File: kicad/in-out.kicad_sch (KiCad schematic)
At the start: 67 parts, among them U3 LM5106MM

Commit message: Most of the main board is done
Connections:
- net C2: no longer names the net of J?.2, R?.1
- net C2: no longer J?.2, R?.1
- removed net C3: J?.2, J?.2, J?.3, J?.3, J?.3, J?.3, TC?.1 (+), TC?.1 (+), TC?.1 (+), TC?.1 (+)
- net VOUT_{SEN} renamed V_{OUT}
- new net: J?.2, J?.3, TC?.1 (+) (x2)
- new net: J?.3, TC?.1 (+) (x2)
- new net: J?.2, R?.1
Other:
- note added: "C1"
- note added: "C1/C2"
- note added: "C2"
- note added: "C3"
- moved on the sheet: R?
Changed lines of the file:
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@@
     (stroke (width 0) (type default))
   )
-  (wire (pts (xy 29.21 35.56) (xy 29.21 33.02))
+  (wire (pts (xy 33.02 35.56) (xy 33.02 31.75))
     (stroke (width 0) (type default))
   )
@@
     (stroke (width 0) (type default))
   )
-  (wire (pts (xy 29.21 22.86) (xy 25.4 22.86))
+  (wire (pts (xy 33.02 21.59) (xy 29.21 21.59))
     (stroke (width 0) (type default))
   )
@@
     (stroke (width 0) (type default))
   )
-  (wire (pts (xy 26.67 67.31) (xy 22.86 67.31))
+  (wire (pts (xy 30.48 66.04) (xy 26.67 66.04))
     (stroke (width 0) (type default))
   )
@@
     (stroke (width 0) (type default))
   )
-  (wire (pts (xy 29.21 25.4) (xy 29.21 22.86))
+  (wire (pts (xy 33.02 24.13) (xy 33.02 21.59))
     (stroke (width 0) (type default))
   )
@@
     (stroke (width 0) (type default))
   )
-  (wire (pts (xy 26.67 80.01) (xy 26.67 77.47))
+  (wire (pts (xy 30.48 80.01) (xy 30.48 76.2))
     (stroke (width 0) (type default))
   )
@@
     (stroke (width 0) (type default))
   )
-  (wire (pts (xy 26.67 69.85) (xy 26.67 67.31))
+  (wire (pts (xy 30.48 68.58) (xy 30.48 66.04))
     (stroke (width 0) (type default))
   )
@@
     (stroke (width 0) (type default))
   )
-  (wire (pts (xy 26.67 80.01) (xy 30.48 80.01))
-    (stroke (width 0) (type default))
-  )
   (wire (pts (xy 229.87 49.53) (xy 233.68 49.53))
     (stroke (width 0) (type default))
@@
     (stroke (width 0) (type default))
   )
-  (wire (pts (xy 29.21 35.56) (xy 33.02 35.56))
-    (stroke (width 0) (type default))
-  )
   (wire (pts (xy 33.02 35.56) (xy 33.02 39.37))
     (stroke (width 0) (type default))
@@
     (stroke (width 0) (type default))
   )
-  (text "C245" (at 57.15 135.89 0)
-    (effects (font (size 1.27 1.27) (thickness 0.254) bold) (justify left bottom))
+  (text "C3" (at 43.18 137.16 0)
+    (effects (font (size 1.27 1.27)) (justify left bottom))
   )
-  (text "C210" (at 96.52 163.83 0)
-    (effects (font (size 1.27 1.27) (thickness 0.254) bold) (justify right bottom))
+  (text "C3" (at 43.18 167.64 0)
+    (effects (font (size 1.27 1.27)) (justify left bottom))
   )
-  (text "C470" (at 57.15 166.37 0)
-    (effects (font (size 1.27 1.27) (thickness 0.254) bold) (justify left bottom))
+  (text "C2" (at 43.18 140.97 0)
+    (effects (font (size 1.27 1.27)) (justify left bottom))
   )
-  (text "C115" (at 96.52 132.08 0)
-    (effects (font (size 1.27 1.27) (thickness 0.254) bold) (justify right bottom))
+  (text "C245" (at 57.15 135.89 0)
+    (effects (font (size 1.27 1.27) (thickness 0.254) bold) (justify left bottom))
   )
-  (label "C2" (at 43.18 171.45 0) (fields_autoplaced)
+  (text "C1/C2" (at 106.68 156.21 0)
     (effects (font (size 1.27 1.27)) (justify left bottom))
   )
-  (label "C3" (at 43.18 137.16 0) (fields_autoplaced)
+  (text "C1" (at 43.18 152.4 0)
     (effects (font (size 1.27 1.27)) (justify left bottom))
   )
-  (label "C3" (at 43.18 167.64 0) (fields_autoplaced)
+  (text "C3" (at 115.57 165.1 0)
     (effects (font (size 1.27 1.27)) (justify left bottom))
   )
-  (label "C1{slash}C2" (at 106.68 187.96 0) (fields_autoplaced)
-    (effects (font (size 1.27 1.27)) (justify left bottom))
+  (text "C210" (at 96.52 163.83 0)
+    (effects (font (size 1.27 1.27) (thickness 0.254) bold) (justify right bottom))
   )
-  (label "C3" (at 115.57 133.35 0) (fields_autoplaced)
-    (effects (font (size 1.27 1.27)) (justify left bottom))
+  (text "C470" (at 57.15 166.37 0)
+    (effects (font (size 1.27 1.27) (thickness 0.254) bold) (justify left bottom))
   )
-  (label "C3" (at 115.57 165.1 0) (fields_autoplaced)
+  (text "C2" (at 43.18 171.45 0)
     (effects (font (size 1.27 1.27)) (justify left bottom))
   )
-  (label "C1" (at 43.18 152.4 0) (fields_autoplaced)
-    (effects (font (size 1.27 1.27)) (justify left bottom))
+  (text "C115" (at 96.52 132.08 0)
+    (effects (font (size 1.27 1.27) (thickness 0.254) bold) (justify right bottom))
   )
-  (label "C1" (at 43.18 182.88 0) (fields_autoplaced)
+  (text "C1/C2" (at 106.68 187.96 0)
     (effects (font (size 1.27 1.27)) (justify left bottom))
   )
-  (label "C1{slash}C2" (at 106.68 156.21 0) (fields_autoplaced)
+  (text "C1" (at 43.18 182.88 0)
     (effects (font (size 1.27 1.27)) (justify left bottom))
   )
-  (label "C2" (at 43.18 140.97 0) (fields_autoplaced)
+  (text "C3" (at 115.57 133.35 0)
     (effects (font (size 1.27 1.27)) (justify left bottom))
   )
@@
     (effects (font (size 1.27 1.27)) (justify left))
   )
-  (hierarchical_label "HNDL_{SEN}" (shape input) (at 25.4 22.86 180) (fields_autoplaced)
+  (hierarchical_label "HNDL_{SEN}" (shape input) (at 29.21 21.59 180) (fields_autoplaced)
     (effects (font (size 1.27 1.27)) (justify right))
   )
@@
     (effects (font (size 1.27 1.27)) (justify left))
   )
-  (hierarchical_label "VOUT_{SEN}" (shape input) (at 41.91 57.15 180) (fields_autoplaced)
+  (hierarchical_label "V_{OUT}" (shape input) (at 41.91 57.15 180) (fields_autoplaced)
     (effects (font (size 1.27 1.27)) (justify right))
   )
@@
     (effects (font (size 1.27 1.27)) (justify left))
   )
-  (hierarchical_label "SLEEP_{SEN}" (shape input) (at 22.86 67.31 180) (fields_autoplaced)
+  (hierarchical_label "SLEEP_{SEN}" (shape input) (at 26.67 66.04 180) (fields_autoplaced)
     (effects (font (size 1.27 1.27)) (justify right))
   )
@@
     )
   )
-  (symbol (lib_id "Device:R") (at 29.21 29.21 0) (unit 1)
+  (symbol (lib_id "Device:R") (at 33.02 27.94 0) (unit 1)
     (in_bom yes) (on_board yes) (dnp no)
-    (property "Reference" "R?" (at 30.48 26.67 0)
+    (property "Reference" "R?" (at 34.29 25.4 0)
       (effects (font (size 1.27 1.27)) (justify left))
     )
-    (property "Value" "220" (at 30.48 31.75 0)
+    (property "Value" "220" (at 34.29 30.48 0)
       (effects (font (size 1.27 1.27)) (justify left))
     )
-    (property "Footprint" "Resistor_SMD:R_0603_1608Metric_Pad0.98x0.95mm_HandSolder" (at 27.432 29.21 90)
+    (property "Footprint" "Resistor_SMD:R_0603_1608Metric_Pad0.98x0.95mm_HandSolder" (at 31.242 27.94 90)
       (effects (font (size 1.27 1.27)) hide)
     )
-    (property "Datasheet" "~" (at 29.21 29.21 0)
+    (property "Datasheet" "~" (at 33.02 27.94 0)
       (effects (font (size 1.27 1.27)) hide)
     )
@@
     )
   )
-  (symbol (lib_id "Device:R") (at 26.67 73.66 0) (unit 1)
+  (symbol (lib_id "Device:R") (at 30.48 72.39 0) (unit 1)
     (in_bom yes) (on_board yes) (dnp no)
-    (property "Reference" "R?" (at 27.94 71.12 0)
+    (property "Reference" "R?" (at 31.75 69.85 0)
       (effects (font (size 1.27 1.27)) (justify left))
     )
-    (property "Value" "220" (at 27.94 76.2 0)
+    (property "Value" "220" (at 31.75 74.93 0)
       (effects (font (size 1.27 1.27)) (justify left))
     )
-    (property "Footprint" "Resistor_SMD:R_0603_1608Metric_Pad0.98x0.95mm_HandSolder" (at 24.892 73.66 90)
+    (property "Footprint" "Resistor_SMD:R_0603_1608Metric_Pad0.98x0.95mm_HandSolder" (at 28.702 72.39 90)
       (effects (font (size 1.27 1.27)) hide)
     )
-    (property "Datasheet" "~" (at 26.67 73.66 0)
+    (property "Datasheet" "~" (at 30.48 72.39 0)
       (effects (font (size 1.27 1.27)) hide)
     )
@@
   )
   (symbol (lib_id "PCM_Diode_Schottky_AKL:B0530WS") (at 63.5 80.01 0) (unit 1)
-    (in_bom yes) (on_board yes) (dnp no) (fields_autoplaced)
+    (in_bom yes) (on_board yes) (dnp no)
     (property "Reference" "D9" (at 63.8175 74.93 0)
       (effects (font (size 1.27 1.27)))

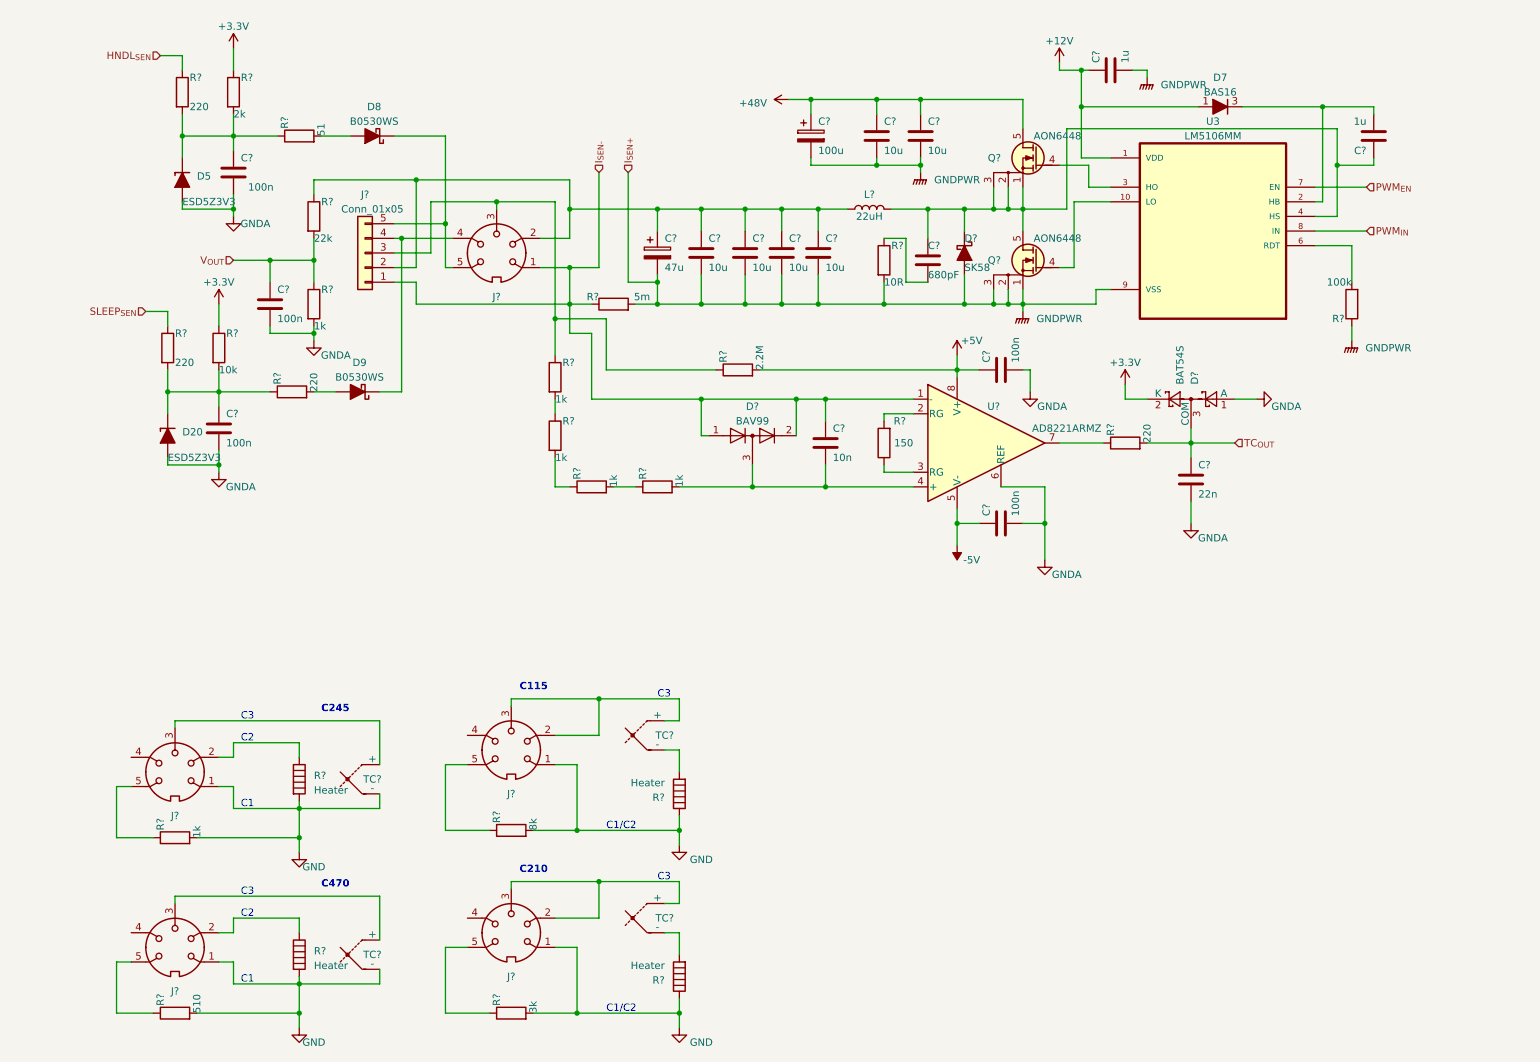
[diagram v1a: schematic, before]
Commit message: Main board: add BT
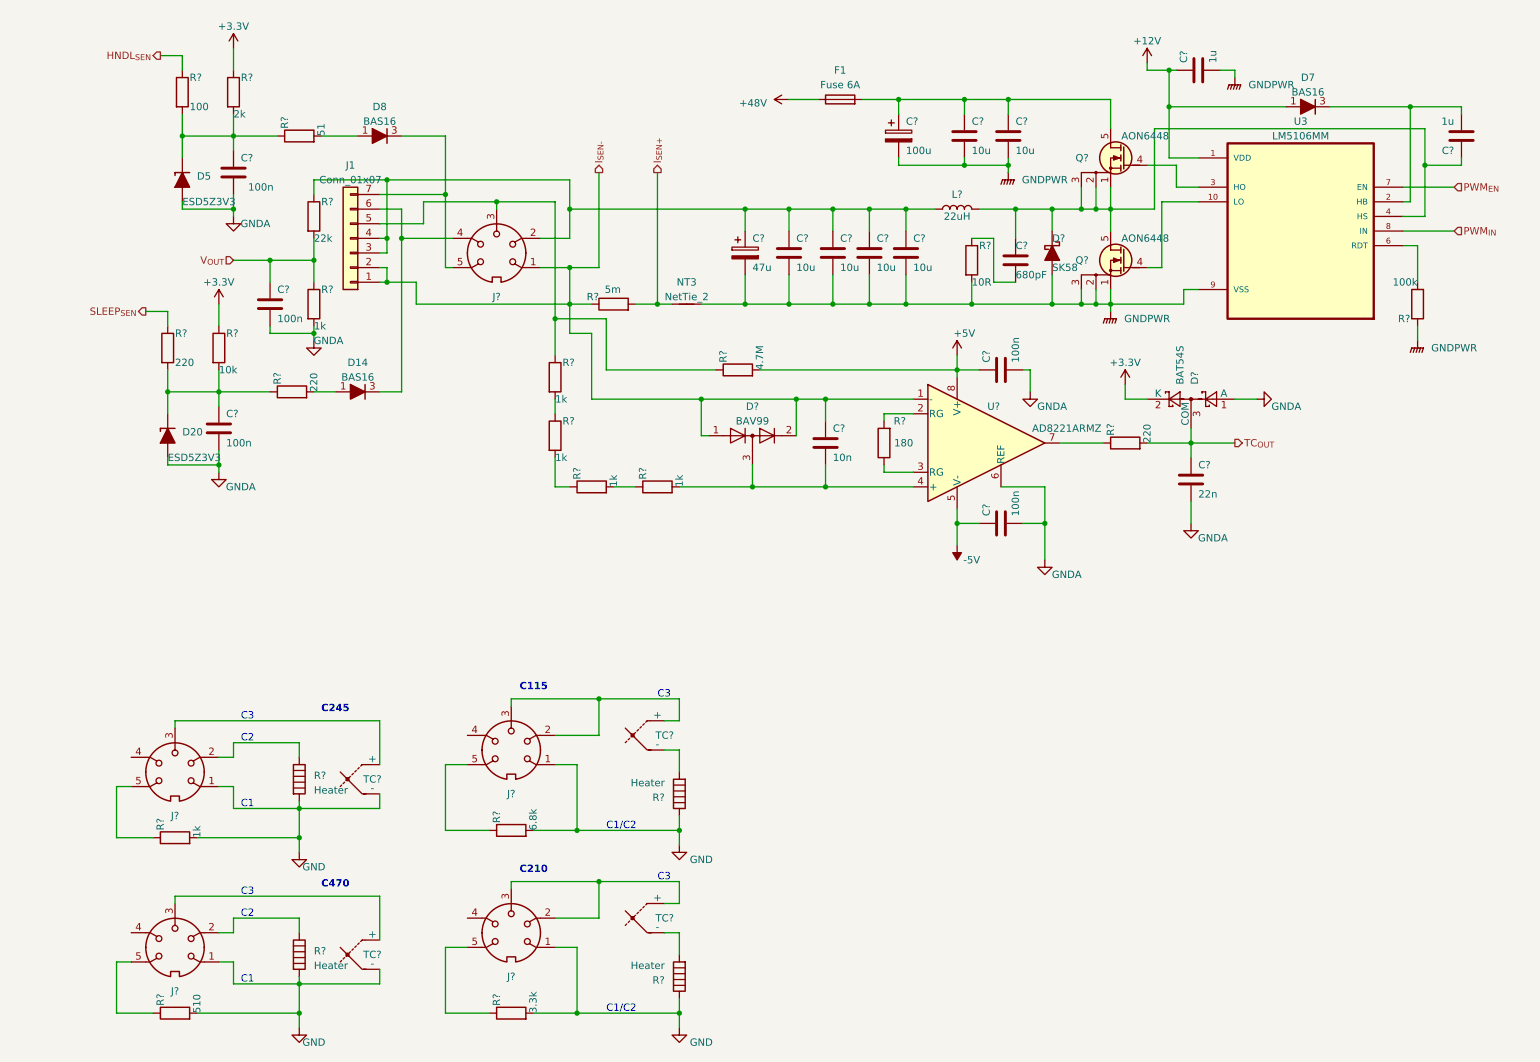
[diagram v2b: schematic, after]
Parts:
- removed D8, D9: B0530WS, PCM_Diode_SMD_AKL:D_SOD-323F, symbol PCM_Diode_Schottky_AKL:B0530WS
- removed J?: Conn_01x05, Connector_JST:JST_EH_B5B-EH-A_1x05_P2.50mm_Vertical, symbol Connector_Generic:Conn_01x05
- added D14, D8: BAS16, Package_TO_SOT_SMD_AKL:SOT-23, symbol Diode_AKL:BAS16
- added F1: Fuse 6A, Fuse:Fuseholder_Littelfuse_Nano2_154x, symbol Device:Fuse
- added J1: Conn_01x07, Connector_JST:JST_EH_B7B-EH-A_1x07_P2.50mm_Vertical, symbol Connector_Generic:Conn_01x07
- added NT3: NetTie_2, NetTie:NetTie-2_SMD_Pad2.0mm, symbol Device:NetTie_2
- C?: footprint Capacitor_SMD:C_0805_2012Metric -> Capacitor_THT:C_Radial_D8.0mm_H11.5mm_P3.50mm
- C? (x5): footprint Capacitor_SMD:C_0805_2012Metric -> Capacitor_SMD:C_0603_1608Metric_Pad1.08x0.95mm_HandSolder
- C?: footprint Inductor_SMD:L_Bourns_SRP1770TA_16.9x16.9mm -> Capacitor_THT:C_Radial_D8.0mm_H11.5mm_P3.50mm
- D20: footprint PCM_Diode_SMD_AKL:D_SOD-523 -> Diode_SMD:D_SOD-523; symbol PCM_Diode_TVS_AKL:ESD5Z3V3 -> Diode_TVS_AKL:ESD5Z3V3
- D5: footprint PCM_Diode_SMD_AKL:D_SOD-523_TVS -> Diode_SMD_AKL:D_SOD-523_TVS; symbol PCM_Diode_TVS_AKL:ESD5Z3V3 -> Diode_TVS_AKL:ESD5Z3V3
- D7: footprint PCM_Package_TO_SOT_SMD_AKL:SOT-23 -> Package_TO_SOT_SMD_AKL:SOT-23; symbol PCM_Diode_AKL:BAS16 -> Diode_AKL:BAS16
- D?: footprint PCM_Diode_SMD_AKL:D_SMB-SMC_Universal -> Diode_SMD_AKL:D_SMB-SMC_Universal; symbol PCM_Diode_Schottky_AKL:SK58 -> Diode_Schottky_AKL:SK58
- Q? (x2): footprint PCM_Package_SON_AKL:Infineon_PG-TDSON-8 -> Package_SON_AKL:Infineon_PG-TDSON-8; symbol PCM_Transistor_MOSFET_AKL:AON6220 -> Transistor_MOSFET_AKL:AON6220
- R?: value 3k -> 3.3k
- R?: value 220 -> 100
- R?: value 150 -> 180
- R?: value 8k -> 6.8k
- R?: value 2.2M -> 4.7M
- U?: footprint PCM_Package_SO_AKL:MSOP-8_3x3mm_P0.65mm -> Package_SO_AKL:MSOP-8_3x3mm_P0.65mm; symbol PCM_Amplifier_Instrumentation_AKL:AD8221ARMZ -> Amplifier_Instrumentation_AKL:AD8221ARMZ
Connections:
- net +48V: now also F1.1; no longer C?.1, C?.1, C?.1, Q?.5 (D)
- net GNDPWR: now also NT3.2; no longer R?.2
- net I_{SEN-}: now also J1.1 (Pin_1), J1.2 (Pin_2)
- net at J?.3, R?.1, R?.1: now also J1.5 (Pin_5)
- net at R?.2: now also D8.1 (A)
- net at C?.1, C?.1, C?.1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: now also J1.3 (Pin_3), J1.4 (Pin_4)
- net at R?.2: now also D14.1 (A)
- net at J?.4: now also D14.3 (K), J1.6 (Pin_6)
- net at J?.5: now also D8.3 (K), J1.7 (Pin_7)
- new net: C?.1, C?.1, C?.1, F1.2, Q?.5 (D)
- new net I_{SEN+}: NT3.1, R?.2
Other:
- moved on the sheet: C?, D7, D?, L?, Q?, R?, U3

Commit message: PCB routing initial
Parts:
- renumbered D14 to D11, D5 to D25, D20 to D29, F1 to F2, J1 to J9, NT3 to NT4, U3 to U10

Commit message: Route power stage
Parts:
- renumbered U10 to U11
